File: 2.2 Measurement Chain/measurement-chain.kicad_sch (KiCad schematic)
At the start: 22 parts, among them IC1 MAX6126A30+T, J1 M12 5-Pin Socket, U4 AZ1117-ADJ, U5 MAX11270, U6 AD8421

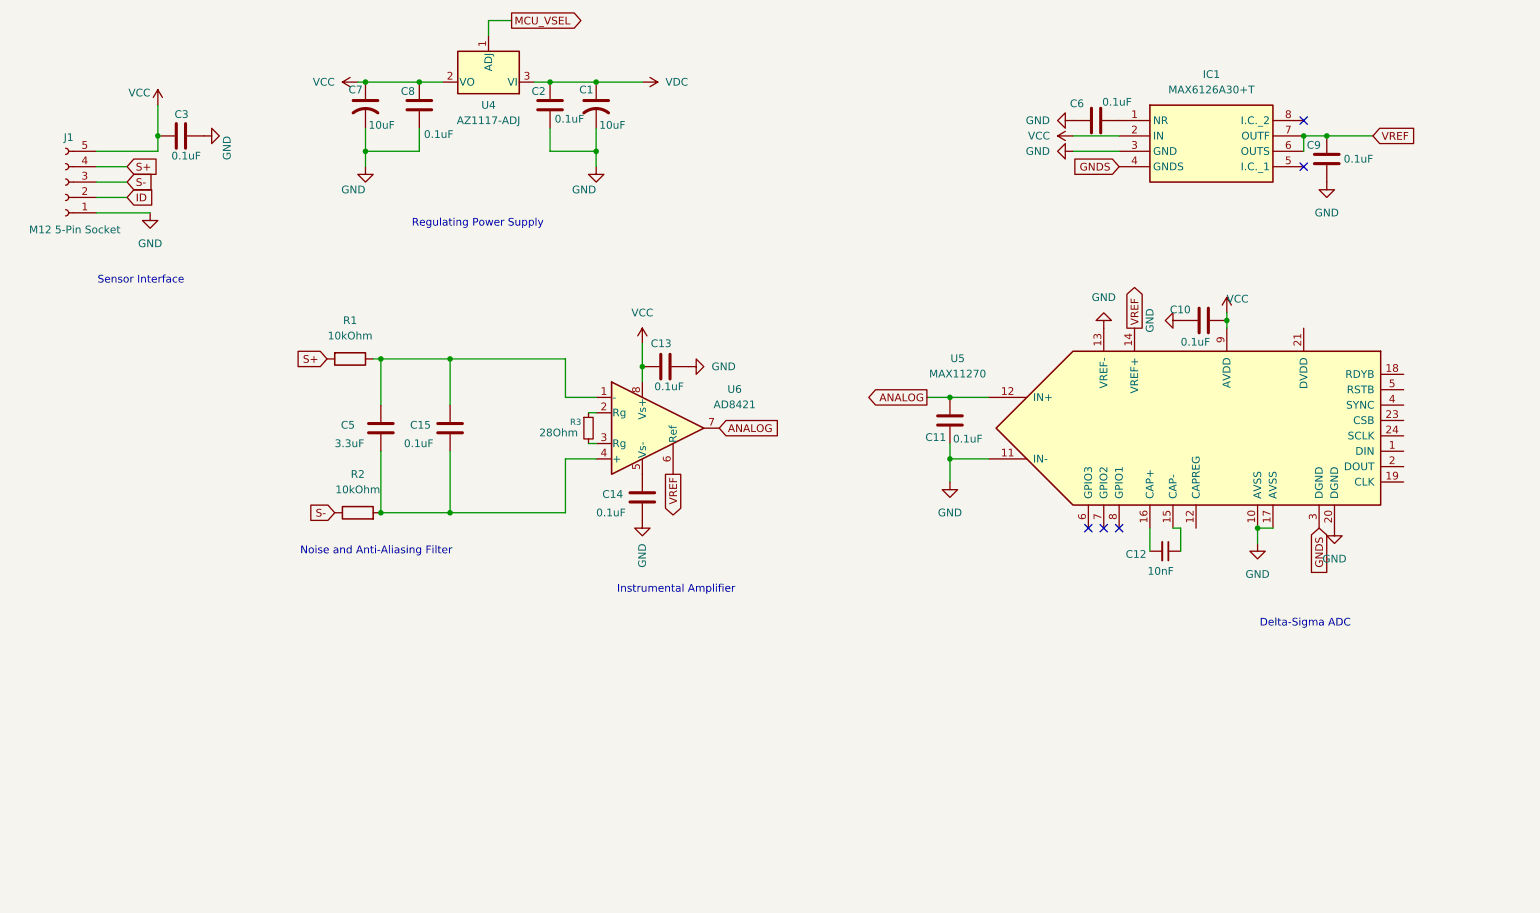
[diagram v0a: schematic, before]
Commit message: Added VGA to solve the gain problem
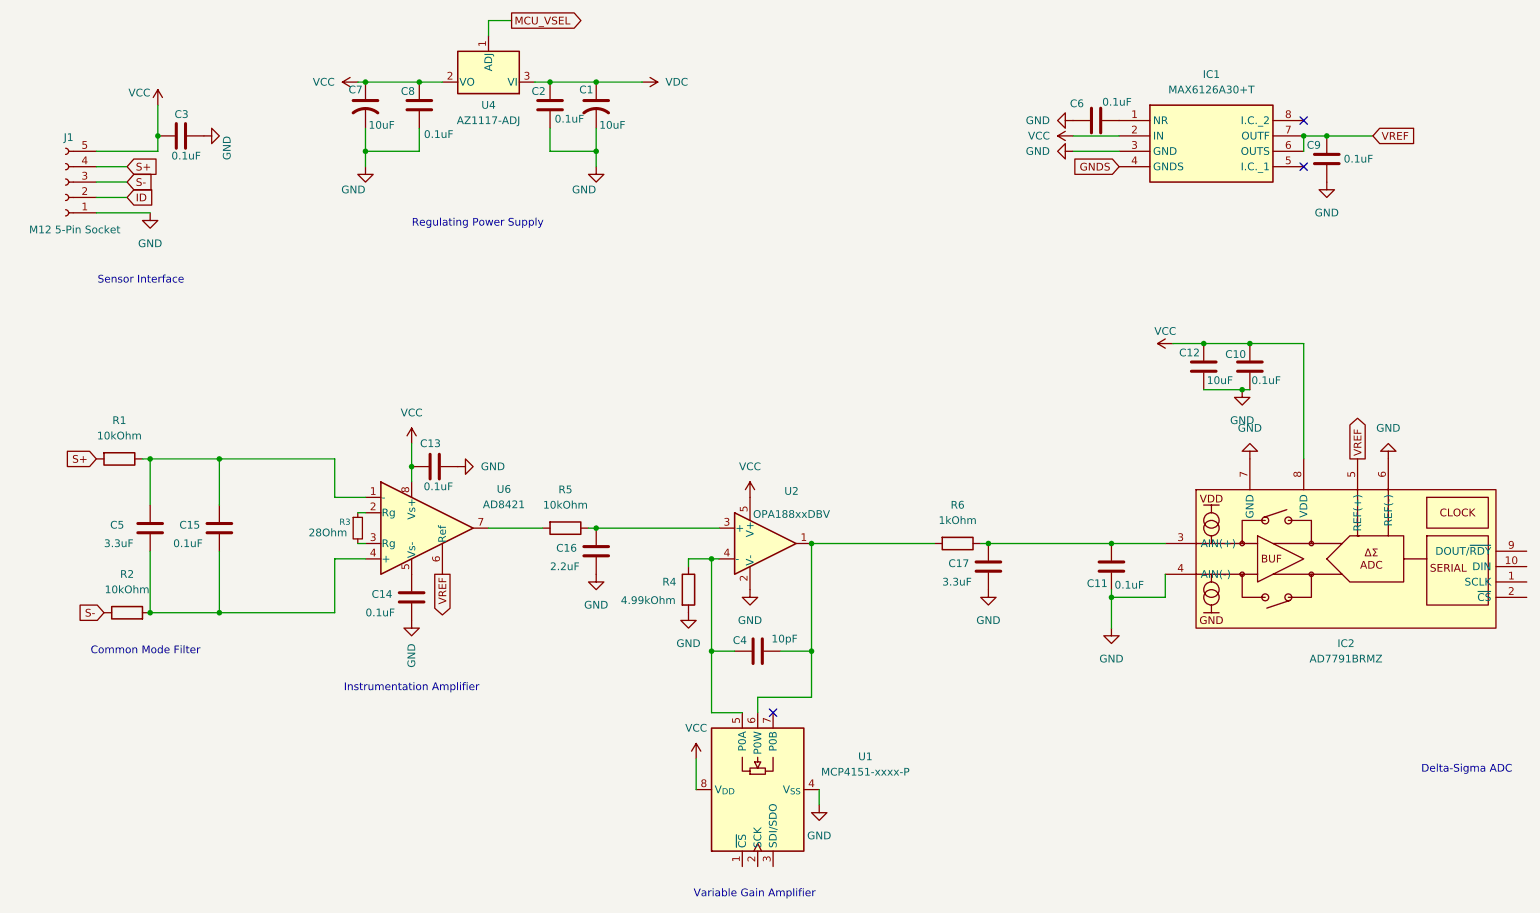
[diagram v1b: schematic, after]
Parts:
- removed C12: 10nF, symbol Device:C_Small
- removed U5: MAX11270, Package_SO:SOIC-8_3.9x4.9mm_P1.27mm, symbol gp-components:MAX11270
- added C12: 10uF, symbol Device:C
- added C16: 2.2uF, symbol Device:C
- added C17: 3.3uF, symbol Device:C
- added C4: 10pF, symbol Device:C
- added IC2: AD7791BRMZ, SOP50P490X110-10N, symbol gp-components:AD7791BRMZ
- added R4: 4.99kOhm, symbol Device:R
- added R5: 10kOhm, symbol Device:R
- added R6: 1kOhm, symbol Device:R
- added U1: MCP4151-xxxx-P, Package_DIP:DIP-8_W7.62mm, symbol Potentiometer_Digital:MCP4151-xxxx-P
- added U2: OPA188xxDBV, Package_TO_SOT_SMD:TSOT-23-5, symbol Amplifier_Operational:OPA188xxDBV
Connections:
- net GND: now also C12.2, C16.2, C17.2, IC2.4 (AIN(-)), IC2.6 (REF(-)), IC2.7 (GND), R4.2, U1.4 (V_{SS}), U2.2 (V-)
- net VCC: now also C12.1, IC2.8 (VDD), U1.8 (V_{DD}), U2.5 (V+)
- net VREF: now also IC2.5 (REF(+))
- net ANALOG: no longer names the net of C11.1
- net ANALOG: now also C17.1, IC2.3 (AIN(+)), R6.1; no longer U6.7
- new net: C16.1, R5.1, U2.3 (+)
- new net: C4.2, R6.2, U1.6 (P0W), U2.1
- new net: C4.1, R4.1, U1.5 (P0A), U2.4 (-)
- new net: R5.2, U6.7
- no-connect marks 5 -> 3
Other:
- note added: "Common Mode Filter"
- note added: "Instrumentation Amplifier"
- note added: "Variable Gain Amplifier"
- note removed: "Instrumental Amplifier"
- note removed: "Noise and Anti-Aliasing Filter"
- moved on the sheet: C10, C11, C13, C14, C15, C5, R1, R2, R3, U6

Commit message: Minor Updates
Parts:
- added C18: 0.47uF, symbol Device:C
- C16: value 2.2uF -> 4.7uF
- C17: value 3.3uF -> 0.33uF
- R5: value 10kOhm -> 4.7kOhm
- R6: value 1kOhm -> 10kOhm
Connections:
- net GND: now also C18.2
- net at C11.1, C17.1, IC2.3 (AIN(+))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: now also C18.1
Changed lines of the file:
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@@
 	)
 	(junction
+		(at 189.23 106.68)
+		(diameter 0)
+		(color 0 0 0 0)
+	)
+	(junction
 		(at 40.64 118.11)
 		(diameter 0)
@@
 	(wire
 		(pts
+			(xy 189.23 106.68) (xy 199.39 106.68)
+		)
+		(stroke
+			(width 0)
+			(type default)
+		)
+	)
+	(wire
+		(pts
 			(xy 106.68 38.1) (xy 106.68 41.91)
 		)
@@
 	(wire
 		(pts
-			(xy 179.07 106.68) (xy 199.39 106.68)
+			(xy 179.07 106.68) (xy 189.23 106.68)
 		)
 		(stroke
@@
 			)
 		)
-		(property "Value" "2.2uF"
+		(property "Value" "4.7uF"
 			(at 106.68 110.49 0)
 			(effects
@@
 			)
 		)
-		(property "Value" "1kOhm"
+		(property "Value" "10kOhm"
 			(at 173.99 102.87 90)
 			(effects
@@
 	)
 	(symbol
+		(lib_id "power:GND")
+		(at 189.23 114.3 0)
+		(unit 1)
+		(exclude_from_sim no)
+		(in_bom yes)
+		(on_board yes)
+		(dnp no)
+		(fields_autoplaced yes)
+		(property "Reference" "#PWR014"
+			(at 189.23 120.65 0)
+			(effects
+				(font
+					(size 1.27 1.27)
+				)
+				(hide yes)
+			)
+		)
+		(property "Value" "GND"
+			(at 189.23 119.38 0)
+			(effects
+				(font
+					(size 1.27 1.27)
+				)
+			)
+		)
+		(property "Footprint" ""
+			(at 189.23 114.3 0)
+			(effects
+				(font
+					(size 1.27 1.27)
+				)
+				(hide yes)
+			)
+		)
+		(property "Datasheet" ""
+			(at 189.23 114.3 0)
+			(effects
+				(font
+					(size 1.27 1.27)
+				)
+				(hide yes)
+			)
+		)
+		(property "Description" "Power symbol creates a global label with name \"GND\" , ground"
+			(at 189.23 114.3 0)
+			(effects
+				(font
+					(size 1.27 1.27)
+				)
+				(hide yes)
+			)
+		)
+		(pin "1"
+		)
+		(instances
+			(project "measurement-chain"
+				(path "/c8cd35e5-2866-4aea-9ab4-10ed472689c0"
+					(reference "#PWR014")
+					(unit 1)
+				)
+			)
+		)
+	)
+	(symbol
 		(lib_id "Device:C")
 		(at 140.97 124.46 90)
@@
 	)
 	(symbol
+		(lib_id "Device:C")
+		(at 189.23 110.49 0)
+		(unit 1)
+		(exclude_from_sim no)
+		(in_bom yes)
+		(on_board yes)
+		(dnp no)
+		(property "Reference" "C18"
+			(at 182.626 109.982 0)
+			(effects
+				(font
+					(size 1.27 1.27)
+				)
+				(justify left)
+			)
+		)
+		(property "Value" "0.47uF"
+			(at 181.61 113.03 0)
+			(effects
+				(font
+					(size 1.27 1.27)
+				)
+				(justify left)
+			)
+		)
+		(property "Footprint" ""
+			(at 190.1952 114.3 0)
+			(effects
+				(font
+					(size 1.27 1.27)
+				)
+				(hide yes)
+			)
+		)
+		(property "Datasheet" "~"
+			(at 189.23 110.49 0)
+			(effects
+				(font
+					(size 1.27 1.27)
+				)
+				(hide yes)
+			)
+		)
+		(property "Description" "Unpolarized capacitor"
+			(at 189.23 110.49 0)
+			(effects
+				(font
+					(size 1.27 1.27)
+				)
+				(hide yes)
+			)
+		)
+		(pin "1"
+		)
+		(pin "2"
+		)
+		(instances
+			(project "measurement-chain"
+				(path "/c8cd35e5-2866-4aea-9ab4-10ed472689c0"
+					(reference "C18")
+					(unit 1)
+				)
+			)
+		)
+	)
+	(symbol
 		(lib_id "power:GND")
 		(at 91.44 93.98 90)
@@
 			)
 		)
-		(property "Value" "10kOhm"
+		(property "Value" "4.7kOhm"
 			(at 109.22 100.33 90)
 			(effects
@@
 			)
 		)
-		(property "Value" "3.3uF"
+		(property "Value" "0.33uF"
 			(at 171.45 113.03 0)
 			(effects
